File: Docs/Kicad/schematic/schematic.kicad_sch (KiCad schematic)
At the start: 30 parts

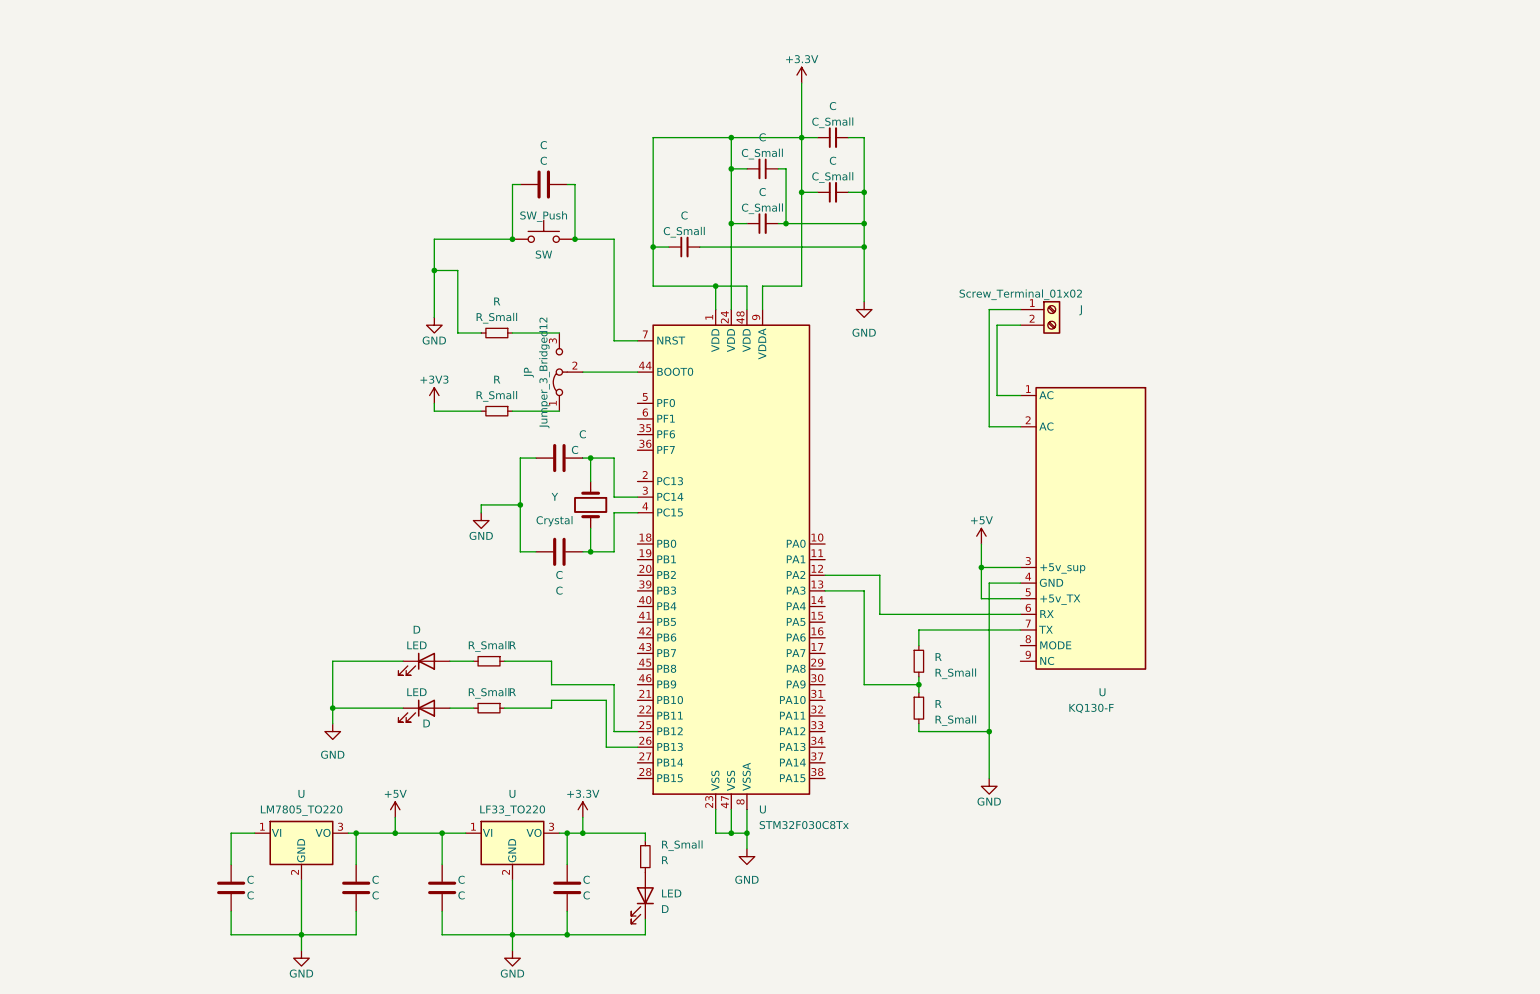
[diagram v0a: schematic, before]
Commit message: Schematic completed
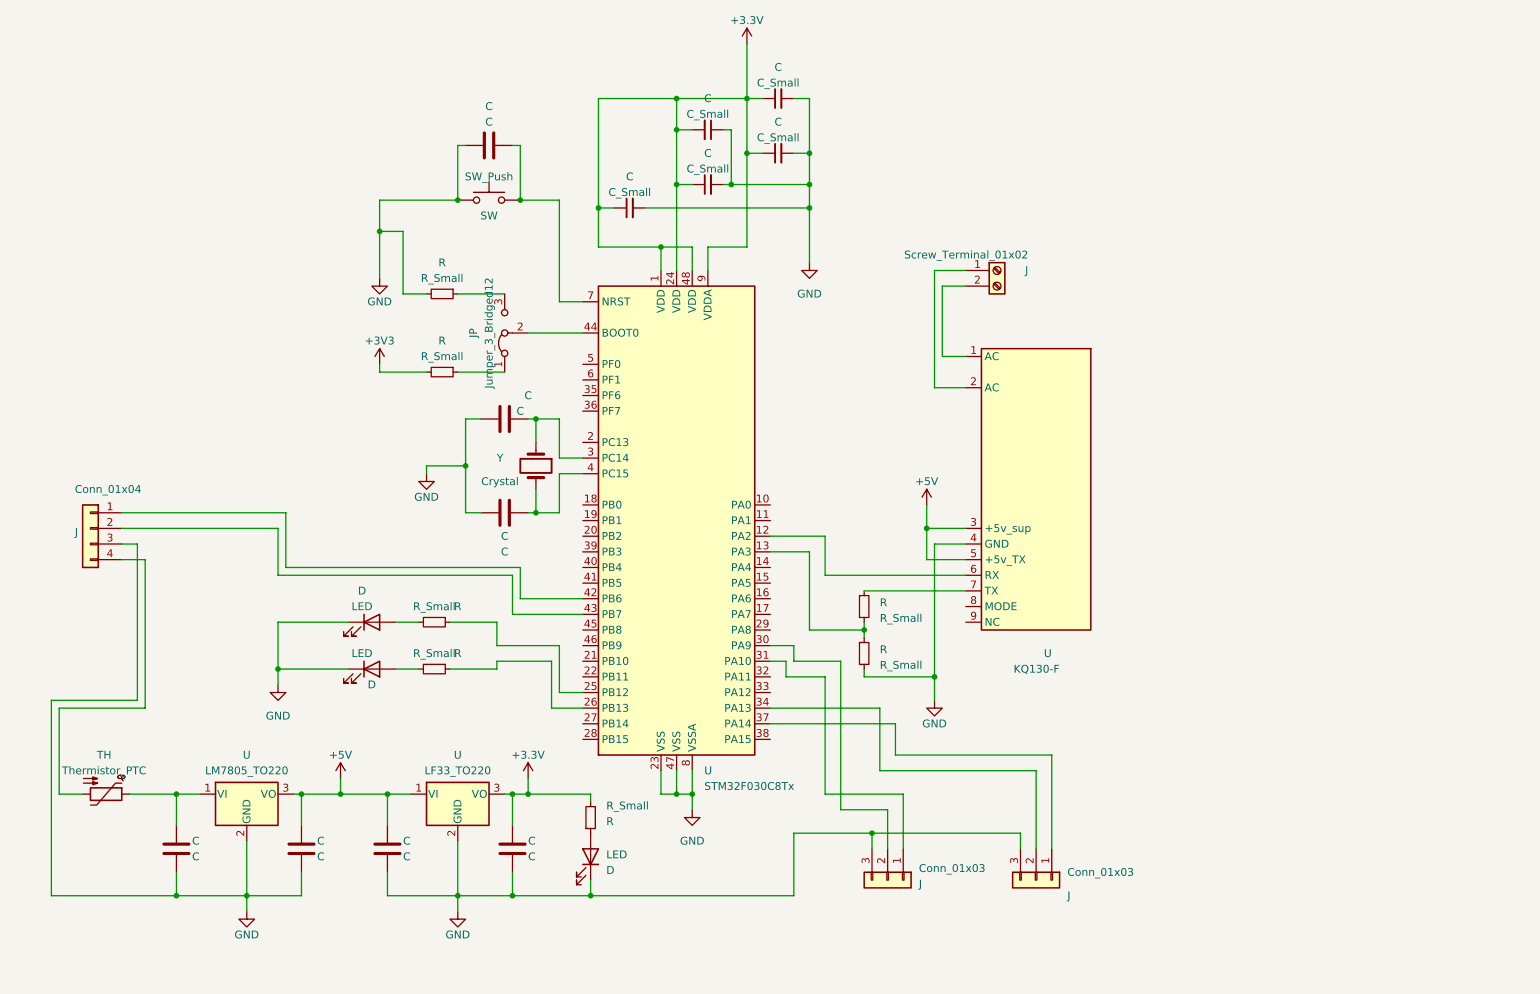
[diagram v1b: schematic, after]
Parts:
- added J (x2): Conn_01x03, symbol Connector_Generic:Conn_01x03
- added J: Conn_01x04, symbol Connector_Generic:Conn_01x04
- added TH: Thermistor_PTC, symbol Device:Thermistor_PTC
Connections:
- net GND: now also J.3 (Pin_3), J.3 (Pin_3), J.3 (Pin_3)
- net at U.30 (PA9): now also J.2 (Pin_2)
- net at U.31 (PA10): now also J.1 (Pin_1)
- net at U.34 (PA13): now also J.2 (Pin_2)
- net at U.37 (PA14): now also J.1 (Pin_1)
- net at U.42 (PB6): now also J.1 (Pin_1)
- net at U.43 (PB7): now also J.2 (Pin_2)
- net at C.1, U.1 (VI): now also TH.1
- new net: J.4 (Pin_4), TH.2
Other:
- company: (none) -> Individual Properiarity
- title: (none) -> plNIC Schematic
- moved on the sheet: C, D, J, JP, R, SW, U, Y

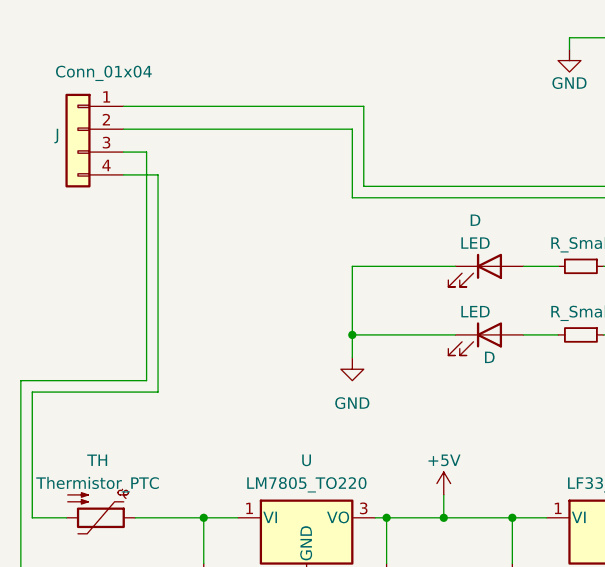
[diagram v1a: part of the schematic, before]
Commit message: Schematic revised and unidirectionalize diode added
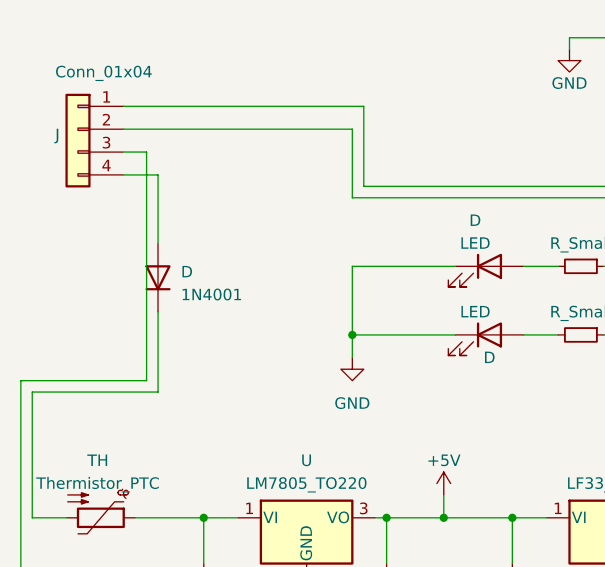
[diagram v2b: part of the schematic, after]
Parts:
- added D: 1N4001, Diode_THT:D_DO-41_SOD81_P10.16mm_Horizontal, symbol Diode:1N4001
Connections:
- net at J.4 (Pin_4): now also D.2 (A); no longer TH.2
- new net: D.1 (K), TH.2
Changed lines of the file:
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@@
     (stroke (width 0) (type default))
   )
-  (wire (pts (xy 57.15 102.87) (xy 57.15 127))
+  (wire (pts (xy 57.15 102.87) (xy 57.15 110.49))
     (stroke (width 0) (type default))
   )
@@
   )
   (wire (pts (xy 151.13 33.02) (xy 152.4 33.02))
+    (stroke (width 0) (type default))
+  )
+  (wire (pts (xy 57.15 118.11) (xy 57.15 127))
     (stroke (width 0) (type default))
   )
@@
     (pin "2")
   )
+  (symbol (lib_id "Diode:1N4001") (at 57.15 114.3 90) (unit 1)
+    (in_bom yes) (on_board yes) (fields_autoplaced)
+    (default_instance (reference "D") (unit 1) (value "1N4001") (footprint "Diode_THT:D_DO-41_SOD81_P10.16mm_Horizontal"))
+    (property "Reference" "D" (id 0) (at 59.69 113.665 90)
+      (effects (font (size 1.27 1.27)) (justify right))
+    )
+    (property "Value" "1N4001" (id 1) (at 59.69 116.205 90)
+      (effects (font (size 1.27 1.27)) (justify right))
+    )
+    (property "Footprint" "Diode_THT:D_DO-41_SOD81_P10.16mm_Horizontal" (id 2) (at 61.595 114.3 0)
+      (effects (font (size 1.27 1.27)) hide)
+    )
+    (property "Datasheet" "http://www.vishay.com/docs/88503/1n4001.pdf" (id 3) (at 57.15 114.3 0)
+      (effects (font (size 1.27 1.27)) hide)
+    )
+    (pin "1")
+    (pin "2")
+  )
   (symbol (lib_id "Device:C") (at 62.23 149.86 0) (unit 1)
     (in_bom yes) (on_board yes)
@@
       (reference "D3") (unit 1) (value "RED") (footprint "")
     )
+    (path "/700ab15f-7927-4675-895c-e1f69e718aeb"
+      (reference "D4") (unit 1) (value "1N4001") (footprint "Diode_THT:D_DO-41_SOD81_P10.16mm_Horizontal")
+    )
     (path "/9372c176-80d0-4898-95d7-8f57f2c8a18f"

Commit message: Schematic revisioned
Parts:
- removed C (x2): C, symbol Device:C
- added C (x2): C, symbol Device:C
- added Q (x2): BC327, Package_TO_SOT_THT:TO-92_Inline, symbol Transistor_BJT:BC327
- added R (x2): R_Small, symbol Device:R_Small
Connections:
- net +5V: now also C.1, Q.3 (E), Q.3 (E)
- net GND: now also C.2, C.2
- net at U.12 (PA2), U.6 (RX): now also R.1
- net at U.25 (PB12): no longer R.1
- net at U.26 (PB13): no longer R.1
- net at R.1, U.7 (TX): now also R.1
- net at TH.1, U.1 (VI): now also C.1
- new net: Q.1 (C), R.1 (x2)
- new net: Q.2 (B), R.2 (x2)
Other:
- moved on the sheet: C, D, J, R, TH, U

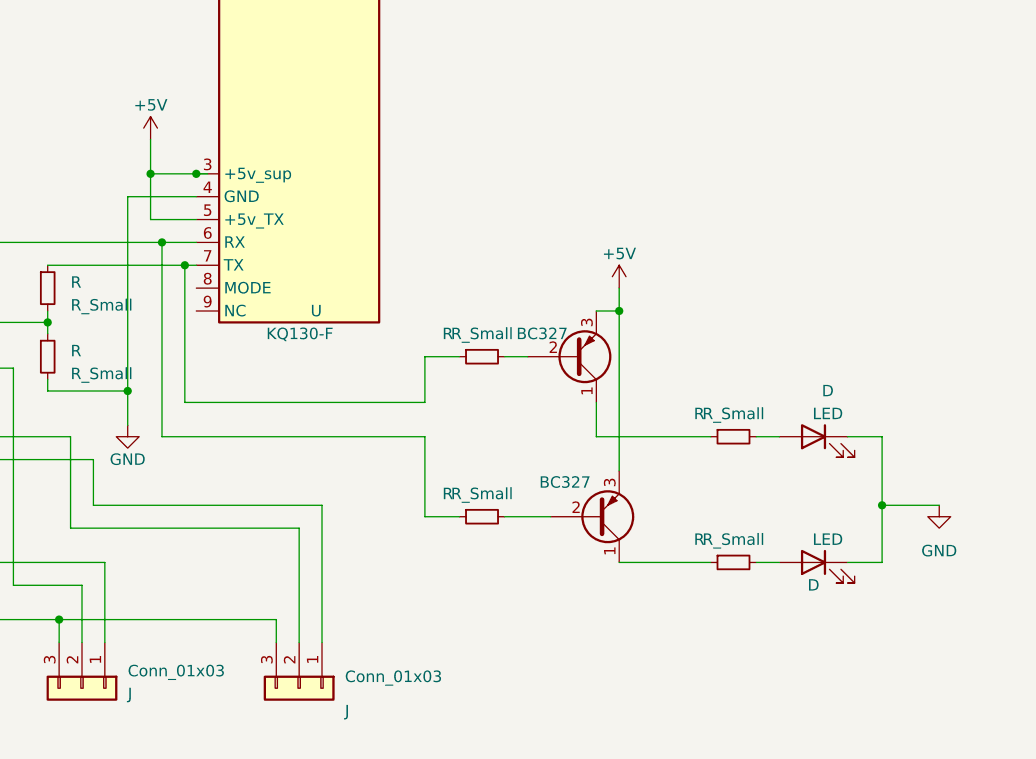
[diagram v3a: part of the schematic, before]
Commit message: Board v1.4 schematic svg and jpg is added
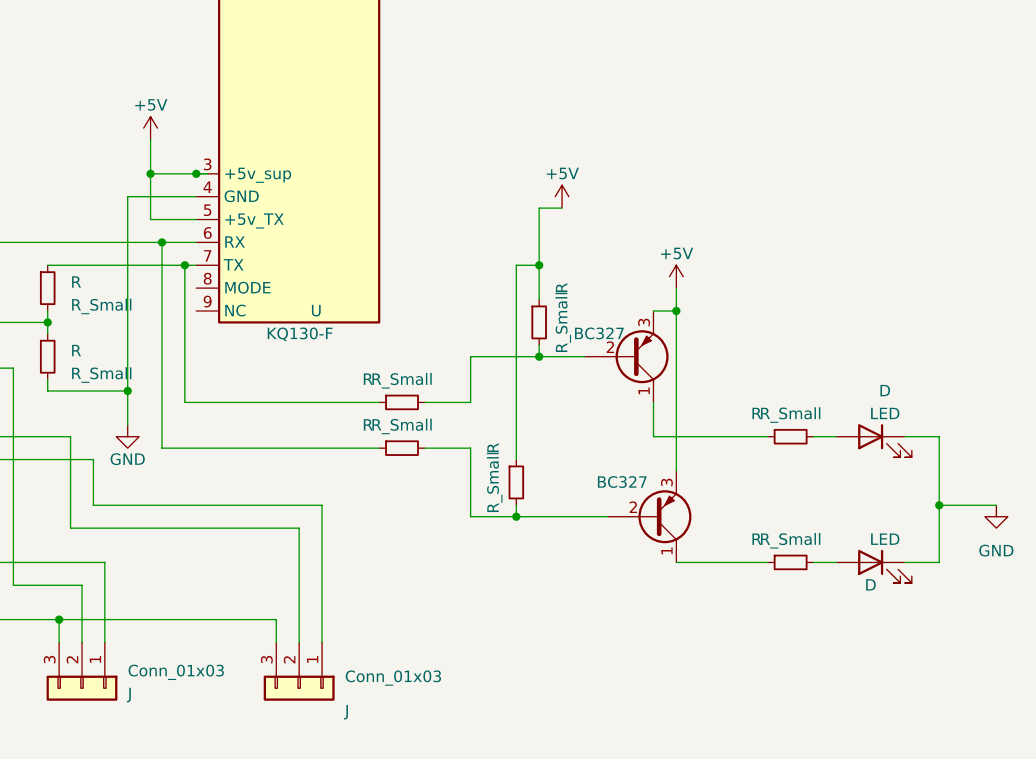
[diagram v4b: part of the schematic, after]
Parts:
- added R (x2): R_Small, symbol Device:R_Small
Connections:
- net +5V: now also R.1, R.1
- net at Q.2 (B), R.2: now also R.2 (x2)
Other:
- moved on the sheet: D, R
